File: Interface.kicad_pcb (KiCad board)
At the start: 4 copper layers, 126.8 x 95.1 mm, 92 parts, among them J101 AudioJack4, J102 switch, J3 TYPE-C-31-M-12, J4 CONN_DISPLAY, Q1 2N7002VC-7, Q2 2N7002VC-7, U1 W25Q128JVPIQ, U2 RP2040, U3 XC6210B332MR-G, Y1 12MHz

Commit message: Fix zones
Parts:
- moved J101 0.11 mm to (134.5, 88.0)
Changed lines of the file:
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@@
     )
     (pad_to_mask_clearance 0)
+    (grid_origin 127.75 43)
     (pcbplotparams
       (layerselection 0x00010fc_ffffffff)
@@
   )
   (footprint "Keyboard:TRRS-PJ-320A" (layer "F.Cu")
-    (at 134.6125 87.95 -90)
+    (at 134.5 87.95 -90)
     (property "Sheetfile" "key-matrix.kicad_sch")
     (property "Sheetname" "Left Matrix")
@@
   (segment (start 135.4375 73.0375) (end 134.5375 73.0375) (width 0.15) (layer "B.Cu") (net 44))
   (segment (start 133.767712 77.701973) (end 133.767712 77.982288) (width 0.15) (layer "F.Cu") (net 45))
-  (segment (start 128.4125 83.3375) (end 128.4125 90.25) (width 0.15) (layer "F.Cu") (net 45))
+  (segment (start 134.2745 77.25) (end 134.219685 77.25) (width 0.15) (layer "F.Cu") (net 45))
+  (segment (start 128.4125 90.1375) (end 128.3 90.25) (width 0.15) (layer "F.Cu") (net 45))
+  (segment (start 128.4125 83.3375) (end 128.4125 90.1375) (width 0.15) (layer "F.Cu") (net 45))
   (segment (start 133.767712 77.982288) (end 128.4125 83.3375) (width 0.15) (layer "F.Cu") (net 45))
   (segment (start 134.219685 77.25) (end 133.767712 77.701973) (width 0.15) (layer "F.Cu") (net 45))
-  (segment (start 134.2745 77.25) (end 134.219685 77.25) (width 0.15) (layer "F.Cu") (net 45))
   (via (at 134.2745 77.25) (size 0.5) (drill 0.3) (layers "F.Cu" "B.Cu") (net 45))
   (segment (start 134.2745 77.25) (end 134.2 77.1755) (width 0.15) (layer "B.Cu") (net 45))
   (segment (start 134.2 77.1755) (end 134.2 75.875) (width 0.15) (layer "B.Cu") (net 45))
+  (segment (start 131.3 87.45) (end 131.3 90.25) (width 0.15) (layer "F.Cu") (net 46))
+  (segment (start 134.242712 84.507288) (end 131.3 87.45) (width 0.15) (layer "F.Cu") (net 46))
   (segment (start 134.242712 77.898725) (end 134.242712 84.507288) (width 0.15) (layer "F.Cu") (net 46))
-  (segment (start 134.242712 84.507288) (end 131.4125 87.3375) (width 0.15) (layer "F.Cu") (net 46))
-  (segment (start 131.4125 87.3375) (end 131.4125 90.25) (width 0.15) (layer "F.Cu") (net 46))
   (via (at 134.242712 77.898725) (size 0.5) (drill 0.3) (layers "F.Cu" "B.Cu") (net 46))
   (segment (start 134.242712 77.892712) (end 133.8 77.45) (width 0.15) (layer "B.Cu") (net 46))
@@
     (polygon
       (pts
-        (xy 139.2 47.5)
-        (xy 139.2 50.9)
+        (xy 128 44.25)
+        (xy 128 46.75)
+        (xy 147.25 46.75)
         (xy 147.3 50.9)
         (xy 147.2 65.8)
@@
         (xy 137.75 78)
         (xy 133.5 82.75)
-        (xy 133.5 102.1)
-        (xy 124.5 102.1)
+        (xy 133.5 102.25)
+        (xy 124.5 102.25)
         (xy 122.25 99.75)
         (xy 122.25 97.25)
-        (xy 122.25 47.75)
+        (xy 122.25 44.25)
       )
     )
@@
     (polygon
       (pts
-        (xy 79.6 37.9)
-        (xy 129.3 38.1)
-        (xy 129.3 45)
-        (xy 139.3 45)
-        (xy 139.3 38.1)
-        (xy 143.5 38.1)
-        (xy 147.7 38.3)
-        (xy 149.1 41.1)
-        (xy 149 75.3)
-        (xy 147 78.3)
-        (xy 140.6 79.6)
-        (xy 136.8 82.2)
-        (xy 134.7 88.1)
-        (xy 134.3 107.4)
-        (xy 125.9 124.9)
-        (xy 122.2 127.6)
-        (xy 118.6 127.7)
-        (xy 102.6 121.9)
-        (xy 78.5 113.5)
-        (xy 59 109.4)
-        (xy 41.5 108.1)
-        (xy 22.4 108)
-        (xy 22.4 50.9)
-        (xy 41.5 50.9)
-        (xy 41.5 37.9)
-        (xy 60.5 37.9)
-        (xy 60.5 31.9)
-        (xy 79.6 31.9)
+        (xy 124.5 102.25)
+        (xy 122.25 99.75)
+        (xy 122.25 75.5)
+        (xy 119.75 75.5)
+        (xy 119.75 70.25)
+        (xy 122.25 70.25)
+        (xy 122.25 44.25)
+        (xy 126.25 44.25)
+        (xy 126.25 43)
+        (xy 127.25 43)
+        (xy 127.25 44.25)
+        (xy 128 44.25)
+        (xy 128 46.75)
+        (xy 129.75 46.75)
+        (xy 129.75 46)
+        (xy 130.75 46)
+        (xy 130.75 46.75)
+        (xy 138.25 46.75)
+        (xy 138.25 46)
+        (xy 139.244231 46)
+        (xy 139.25 46.75)
+        (xy 141 46.75)
+        (xy 141 44.25)
+        (xy 147.25 44.25)
+        (xy 147 78)
+        (xy 137.75 78)
+        (xy 133.5 82.75)
+        (xy 133.5 102.25)
       )
     )

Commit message: add GND vias
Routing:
- net GND: track 42.8 -> 46.6 mm, vias 18 -> 27
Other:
- board text added: "RIGHT"
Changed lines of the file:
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@@
   (gr_arc (start 81.250001 38.749999) (mid 79.835787 38.164213) (end 79.250001 36.749999)
     (stroke (width 0.15) (type default)) (layer "Edge.Cuts"))
-  (gr_text "LEFT" (at 27.75 19.25) (layer "User.1")
+  (gr_text "LEFT" (at 187.5 26) (layer "User.1")
+    (effects (font (size 10 10) (thickness 0.3)))
+  )
+  (gr_text "RIGHT" (at 39.25 21.25) (layer "User.1")
     (effects (font (size 10 10) (thickness 0.3)))
   )
@@
   (segment (start 127.3375 71.8375) (end 127 71.5) (width 0.2) (layer "B.Cu") (net 1))
   (segment (start 137.25 74) (end 137.52 74) (width 0.2) (layer "B.Cu") (net 1))
+  (via (at 131 71.5) (size 0.5) (drill 0.3) (layers "F.Cu" "B.Cu") (net 2))
   (via (at 137.5 77.25) (size 0.5) (drill 0.3) (layers "F.Cu" "B.Cu") (net 2))
   (via (at 126.7 43.65) (size 0.5) (drill 0.3) (layers "F.Cu" "B.Cu") (net 2))
+  (via (at 131 73.5) (size 0.5) (drill 0.3) (layers "F.Cu" "B.Cu") (net 2))
   (via (at 138.06 62.5) (size 0.5) (drill 0.3) (layers "F.Cu" "B.Cu") (net 2))
   (via (at 123.25 95.5) (size 0.5) (drill 0.3) (layers "F.Cu" "B.Cu") (net 2))
   (via (at 130.25 96.5) (size 0.5) (drill 0.3) (layers "F.Cu" "B.Cu") (net 2))
+  (via (at 132 73.5) (size 0.5) (drill 0.3) (layers "F.Cu" "B.Cu") (net 2))
   (via (at 146.5 68.5) (size 0.5) (drill 0.3) (layers "F.Cu" "B.Cu") (net 2))
+  (via (at 132 71.5) (size 0.5) (drill 0.3) (layers "F.Cu" "B.Cu") (net 2))
   (via (at 135.25 66.52) (size 0.5) (drill 0.3) (layers "F.Cu" "B.Cu") (net 2))
   (via (at 142.25 49.5) (size 0.5) (drill 0.3) (layers "F.Cu" "B.Cu") (net 2))
   (via (at 145.5 52.25) (size 0.5) (drill 0.3) (layers "F.Cu" "B.Cu") (net 2))
+  (via (at 133 72.5) (size 0.5) (drill 0.3) (layers "F.Cu" "B.Cu") (net 2))
   (via (at 142.75 72.25) (size 0.5) (drill 0.3) (layers "F.Cu" "B.Cu") (net 2))
   (via (at 130.25 46.5) (size 0.5) (drill 0.3) (layers "F.Cu" "B.Cu") (net 2))
+  (via (at 131 72.5) (size 0.5) (drill 0.3) (layers "F.Cu" "B.Cu") (net 2))
+  (via (at 133 71.5) (size 0.5) (drill 0.3) (layers "F.Cu" "B.Cu") (net 2))
   (via (at 130.5 66.24) (size 0.5) (drill 0.3) (layers "F.Cu" "B.Cu") (net 2))
   (via (at 138.76 46.5) (size 0.5) (drill 0.3) (layers "F.Cu" "B.Cu") (net 2))
   (via (at 138 50.5) (size 0.5) (drill 0.3) (layers "F.Cu" "B.Cu") (net 2))
   (via (at 131.26375 81.7125) (size 0.5) (drill 0.3) (layers "F.Cu" "B.Cu") (net 2))
+  (via (at 133 73.5) (size 0.5) (drill 0.3) (layers "F.Cu" "B.Cu") (net 2))
+  (via (at 132 72.4375) (size 0.5) (drill 0.3) (layers "F.Cu" "B.Cu") (net 2))
   (via (at 131.75 79) (size 0.5) (drill 0.3) (layers "F.Cu" "B.Cu") (net 2))
   (via (at 120.375 73.25) (size 0.5) (drill 0.3) (layers "F.Cu" "B.Cu") (net 2))
@@
   (segment (start 138.025 50.525) (end 139 50.525) (width 0.2) (layer "B.Cu") (net 2))
   (segment (start 139.5 47.75) (end 138.76 47.75) (width 0.3) (layer "B.Cu") (net 2))
+  (segment (start 131 73.4375) (end 128.5625 73.4375) (width 0.2) (layer "B.Cu") (net 2))
   (segment (start 123.25 94.51) (end 123.25 95.5) (width 0.3) (layer "B.Cu") (net 2))
   (segment (start 130 98) (end 129.25 98) (width 0.3) (layer "B.Cu") (net 2))
@@
   (segment (start 146.405 68.595) (end 146.5 68.5) (width 0.3) (layer "B.Cu") (net 2))
   (segment (start 138 50.5) (end 138.025 50.525) (width 0.2) (layer "B.Cu") (net 2))
+  (segment (start 132 72.4375) (end 131 73.4375) (width 0.2) (layer "B.Cu") (net 2))
   (segment (start 125 96.5) (end 125 96) (width 0.3) (layer "B.Cu") (net 2))
   (segment (start 125.25 96.75) (end 125 96.5) (width 0.3) (layer "B.Cu") (net 2))

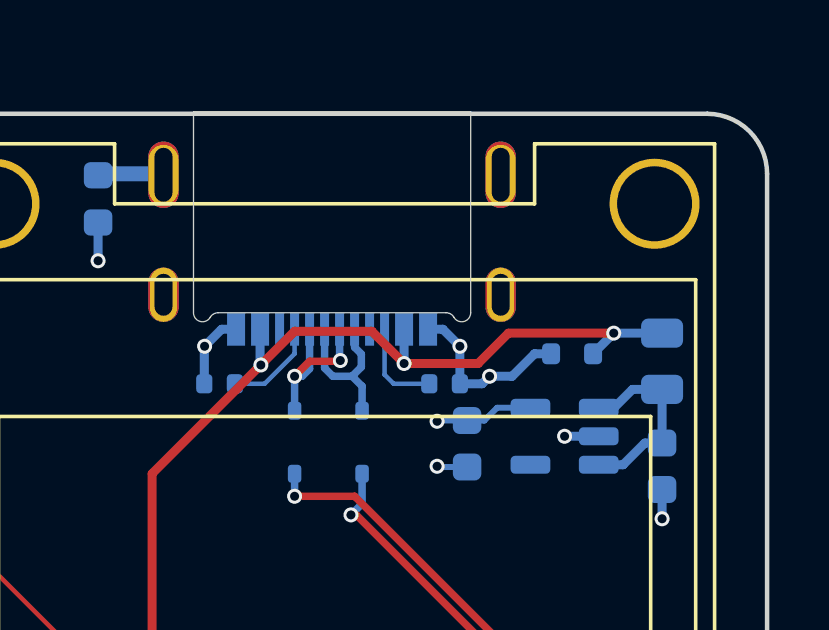
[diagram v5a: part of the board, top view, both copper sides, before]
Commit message: Update to Kicad 8.0
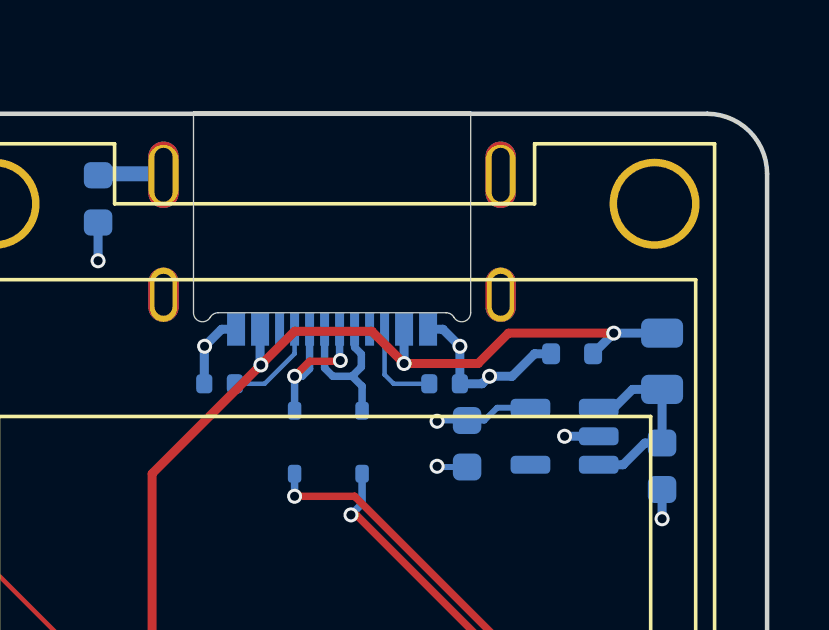
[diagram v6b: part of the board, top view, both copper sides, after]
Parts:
- renumbered locked to D117

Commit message: Update footprints
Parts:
- moved H105 18.1 mm to (108.5, 108.0)
- moved H103 13.3 mm to (118.5, 41.5)
- moved H104 10.2 mm to (79.2, 41.5)
- moved J101 1.92 mm to (132.6, 88.0)
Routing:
- net GND: track 46.6 -> 50.3 mm, vias 27 -> 28
- net /Left MCU/RX: track 15.8 -> 16.6 mm
- net /Left MCU/TX: track 16.9 -> 17.7 mm

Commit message: Complete routing
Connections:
- U2 pad 15: /Left MCU/COL-1 -> unconnected-(U2-GPIO12-Pad15)
- U2 pad 16: /Left MCU/COL-2 -> unconnected-(U2-GPIO13-Pad16)
- U2 pad 17: /Left MCU/COL-3 -> /Left MCU/COL-1
- U2 pad 18: /Left MCU/COL-4 -> /Left MCU/COL-2
- U2 pad 27: /Left MCU/COL-5 -> /Left MCU/COL-3
- U2 pad 28: unconnected-(U2-GPIO17-Pad28) -> /Left MCU/COL-4
- U2 pad 29: unconnected-(U2-GPIO18-Pad29) -> /Left MCU/COL-5
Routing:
- net /Left MCU/QSPI_~{CS}: track 15.7 -> 48.5 mm, vias 0 -> 2
- net /Left MCU/~{RESET}: track 2.11 -> 30.7 mm, vias 0 -> 2
- net /Left MCU/COL-3: track 99.0 -> 104.3 mm
- net /Left MCU/COL-4: track 115.2 -> 119.6 mm
- net /Left MCU/COL-5: track 106.4 -> 110.2 mm
- net GND: track 50.3 -> 51.3 mm, vias 28 -> 29
- net /Left MCU/COL-2: track 121.6 -> 121.1 mm
